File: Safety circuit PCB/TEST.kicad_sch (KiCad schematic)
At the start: 23 parts, among them J1 1053131202, J3 DT13-12PA-B016, Q1 2N7002K, Q2 2N7002K, Q3 2N7002K, Q4 2N7002K, Q5 2N7002K, Q6 2N7002K, Q7 2N7002K

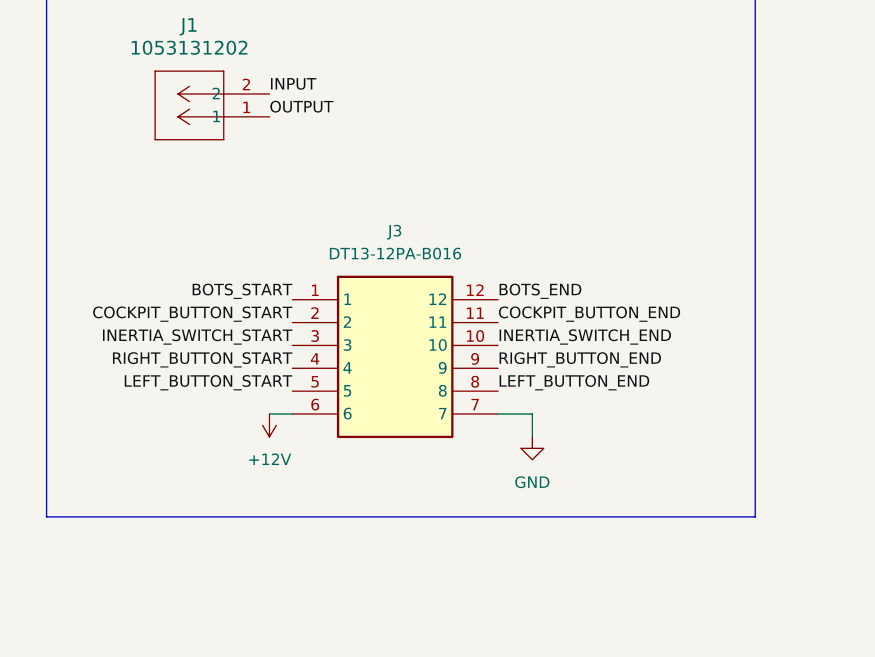
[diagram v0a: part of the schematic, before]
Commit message: 12-Pin connector changed to Molex Nano
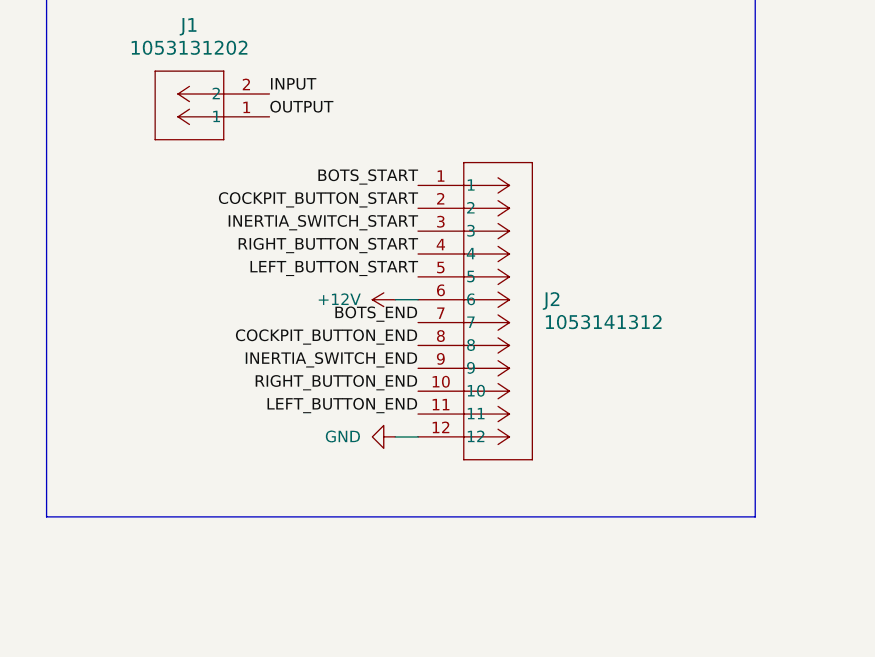
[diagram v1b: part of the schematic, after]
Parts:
- removed J3: DT13-12PA-B016, SC:DT1312PAB016, symbol TEConn:DT13-12PA-B016
- added J2: 1053141312, SC:CONN_SD-105314-100_12_MOL, symbol SC:1053141312
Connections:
- net +12V: now also J2.6
- net BOTS_END: now also J2.7
- net BOTS_START: now also J2.1, J2.8
- net COCKPIT_BUTTON_START: now also J2.2, J2.9
- net GND: now also J2.12
- net INERTIA_SWITCH_START: now also J2.10, J2.3
- net INPUT: now also J2.5
- net LEFT_BUTTON_END: now also J2.11, J2.4
